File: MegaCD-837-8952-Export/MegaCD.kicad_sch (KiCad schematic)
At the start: 182 parts, among them CN1 CON 25P ANGLE, CN2 EDGE 60P, CN3 CON 21P, IC1 68HC000, IC10 65256BLFP-10T, IC11 65256BLFP-10T, IC12 74HC86, IC13 LC8951, IC14 MB8464A-90L, IC15 MB8464A-90L, IC16 MB8464A-10L, IC17 74AC74, IC2 315-5548/315-5632, IC3 315-5476A, IC4 27C1024, IC5 HM514270, IC6 MB3790, IC7 TC511664BZ, IC8 TC511664BZ, IC9 74HC245, J2 2TS, J3 MH, J4 CAS0, M0 TestPoint, M1 TestPoint, M10 TestPoint, M11 TestPoint, M12 TestPoint, M13 TestPoint, M14 TestPoint, M192 TestPoint, M2 TestPoint, M3 TestPoint, M4 TestPoint, M5 TestPoint, M57 TestPoint, M6 TestPoint, M7 TestPoint, M8 TestPoint, M9 TestPoint

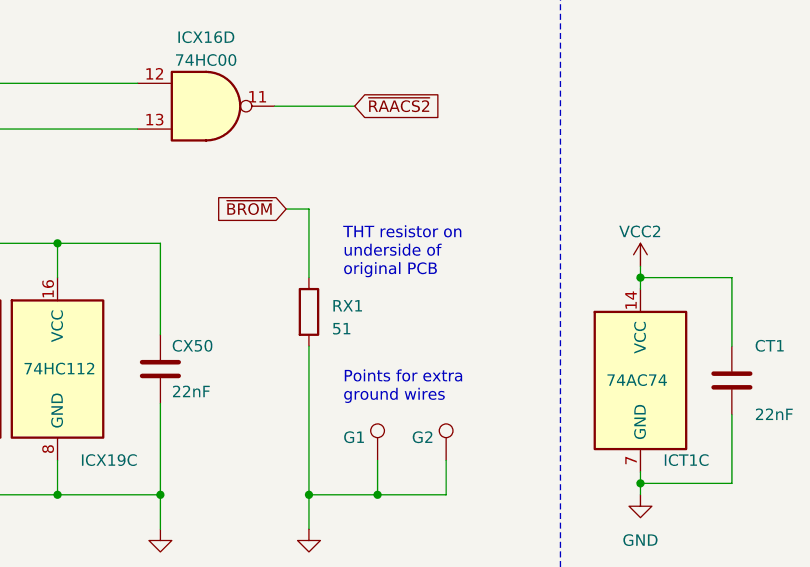
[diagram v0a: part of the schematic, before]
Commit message: THT bodge capacitor was incorrectly marked as a resistor in the 837-8952 schematic.
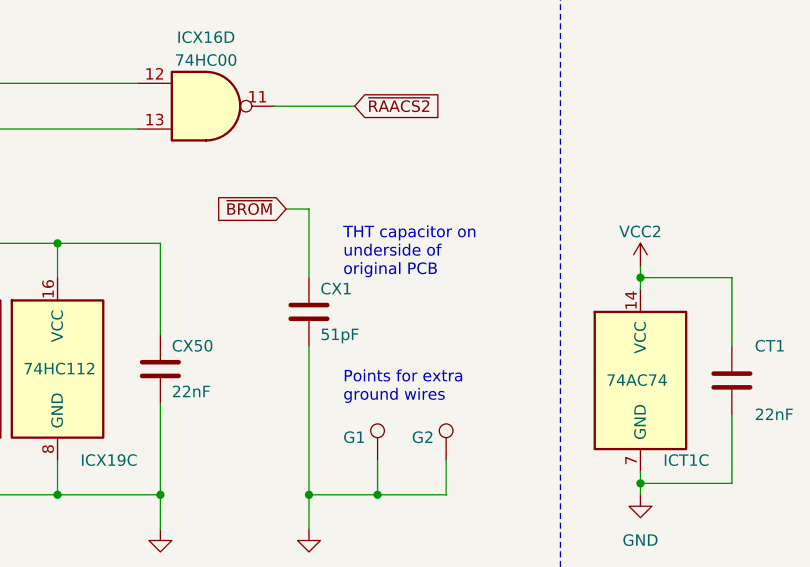
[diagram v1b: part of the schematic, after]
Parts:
- removed RX1: 51, Resistor_THT:R_Axial_DIN0204_L3.6mm_D1.6mm_P7.62mm_Horizontal, symbol Device:R
- added CX1: 51pF, MegaCD_Footprints:SMD_0805_HandSolder, symbol Device:C
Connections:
- net GND: now also CX1.2
- net ~{BROM}: now also CX1.1
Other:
- note added: "THT capacitor on underside of original PCB"
- note removed: "THT resistor on underside of original PCB"
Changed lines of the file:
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@@
     (effects (font (size 2.54 2.54)) (justify left bottom))
   )
-  (text "THT resistor on\nunderside of\noriginal PCB" (at 88.9 539.75 0)
+  (text "THT capacitor on\nunderside of\noriginal PCB" (at 88.9 539.75 0)
     (effects (font (size 1.27 1.27)) (justify left bottom))
   )
@@
     )
   )
+  (symbol (lib_id "Device:C") (at 85.09 543.56 0) (unit 1)
+    (in_bom no) (on_board no) (dnp no)
+    (property "Reference" "CX1" (at 86.36 541.02 0)
+      (effects (font (size 1.27 1.27)) (justify left))
+    )
+    (property "Value" "51pF" (at 86.36 546.1 0)
+      (effects (font (size 1.27 1.27)) (justify left))
+    )
+    (property "Footprint" "MegaCD_Footprints:SMD_0805_HandSolder" (at 86.0552 547.37 0)
+      (effects (font (size 1.27 1.27)) hide)
+    )
+    (property "Datasheet" "~" (at 85.09 543.56 0)
+      (effects (font (size 1.27 1.27)) hide)
+    )
+    (property "Sim.Enable" "0" (at 85.09 543.56 0)
+      (effects (font (size 1.27 1.27)) hide)
+    )
+    (pin "1")
+    (pin "2")
+    (instances
+      (project "MegaCD"
+        (path "/0cd008a0-ed23-4303-a3f0-e3f038adfe31"
+          (reference "CX1") (unit 1)
+        )
+      )
+    )
+  )
   (symbol (lib_id "Device:C_Polarized") (at 560.07 288.29 90) (unit 1)
     (in_bom yes) (on_board yes) (dnp no)
@@
         )
       )
-    )
-  )
-  (symbol (lib_id "Device:R") (at 85.09 543.56 0) (unit 1)
-    (in_bom no) (on_board no) (dnp no)
-    (property "Reference" "RX1" (at 87.63 542.925 0)
-      (effects (font (size 1.27 1.27)) (justify left))
-    )
-    (property "Value" "51" (at 87.63 545.465 0)
-      (effects (font (size 1.27 1.27)) (justify left))
-    )
-    (property "Footprint" "Resistor_THT:R_Axial_DIN0204_L3.6mm_D1.6mm_P7.62mm_Horizontal" (at 83.312 543.56 90)
-      (effects (font (size 1.27 1.27)) hide)
-    )
-    (property "Datasheet" "~" (at 85.09 543.56 0)
-      (effects (font (size 1.27 1.27)) hide)
-    )
-    (property "Sim.Enable" "0" (at 85.09 543.56 0)
-      (effects (font (size 1.27 1.27)) hide)
-    )
-    (pin "1")
-    (pin "2")
-    (instances
-      (project "MegaCD"
-        (path "/0cd008a0-ed23-4303-a3f0-e3f038adfe31"
-          (reference "RX1") (unit 1)
-        )
-      )
